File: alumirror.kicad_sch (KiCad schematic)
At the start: 36 parts, among them J1 USB_C_Receptacle_USB2.0_16P_2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, J2 USB_C_Receptacle_USB2.0_16P_2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, J3 USB_C_Receptacle_USB2.0_16P_2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, J4 USB_C_Receptacle_USB2.0_16P_2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, SW1 BOOT, U1 CH552T, U2 CH552T, U3 USBLC6-2P6, U4 USBLC6-2P6, U5 USBLC6-2P6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

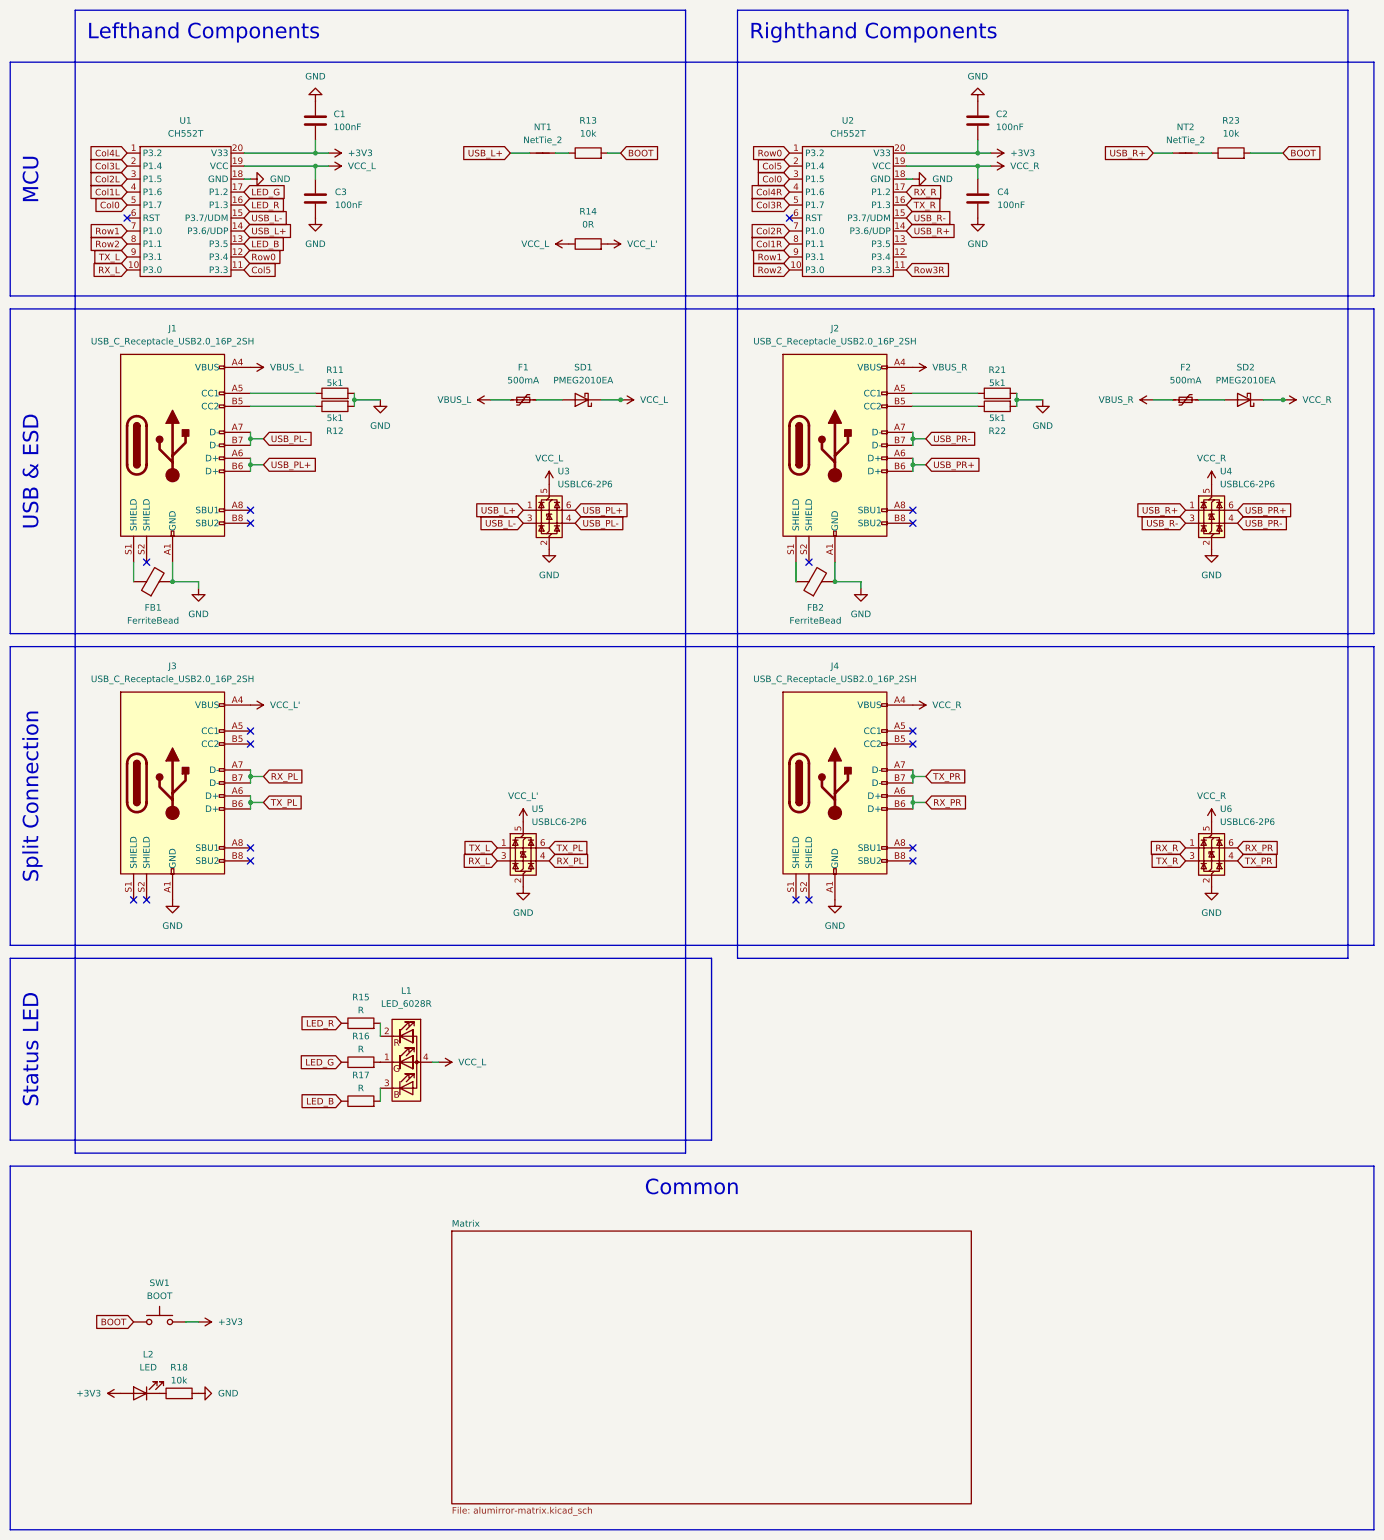
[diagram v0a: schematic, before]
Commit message: Rearrange components for better layout
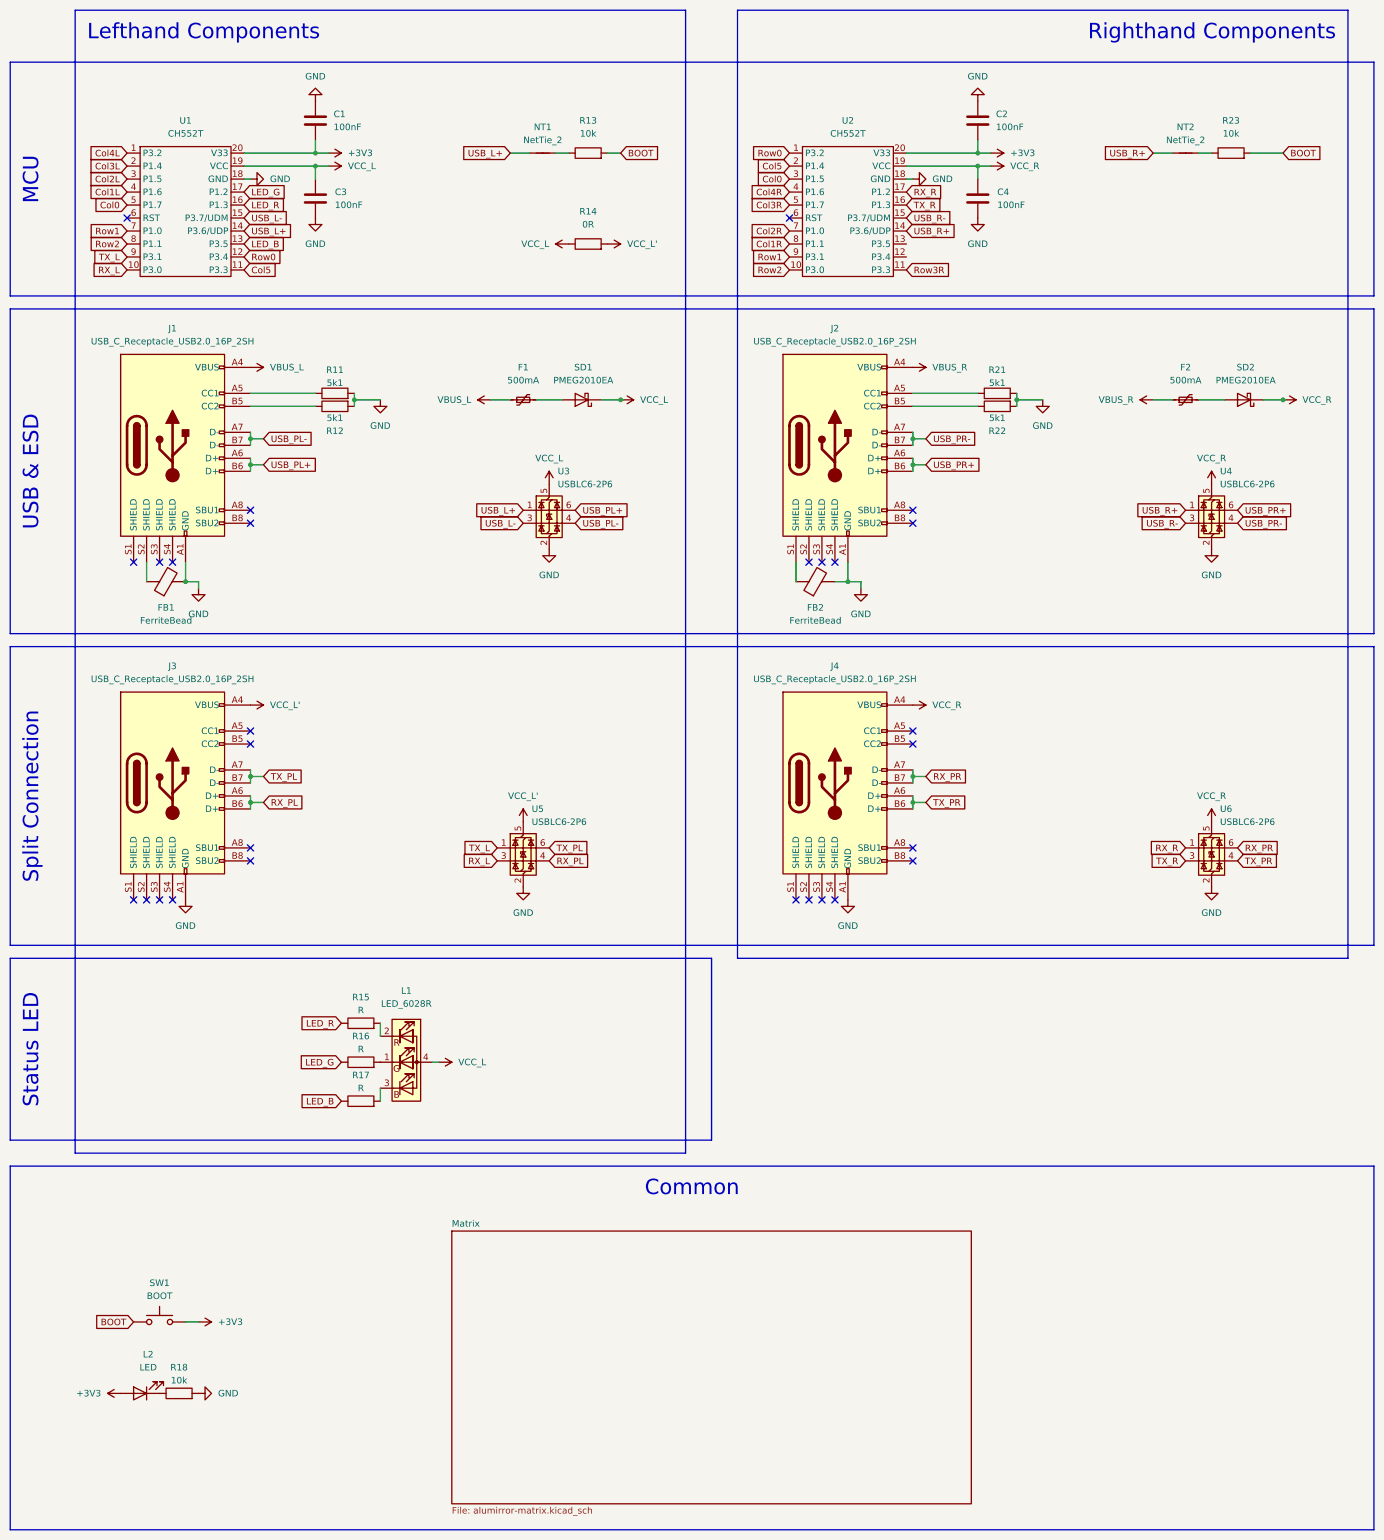
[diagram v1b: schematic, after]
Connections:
- net RX_PL: now also J3.A6 (D+), J3.B6 (D+); no longer J3.A7 (D-), J3.B7 (D-)
- net RX_PR: now also J4.A7 (D-), J4.B7 (D-); no longer J4.A6 (D+), J4.B6 (D+)
- net TX_PL: now also J3.A7 (D-), J3.B7 (D-); no longer J3.A6 (D+), J3.B6 (D+)
- net TX_PR: now also J4.A6 (D+), J4.B6 (D+); no longer J4.A7 (D-), J4.B7 (D-)
- net at FB1.1: now also J1.S2 (SHIELD); no longer J1.S1 (SHIELD)
- no-connect marks 20 -> 28
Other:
- moved on the sheet: FB1
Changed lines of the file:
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@@
 	)
 	(junction
-		(at 62.23 165.1)
+		(at 179.07 127)
 		(diameter 0)
 		(color 0 0 0 0)
 	)
 	(junction
-		(at 62.23 170.18)
+		(at 62.23 165.1)
 		(diameter 0)
 		(color 0 0 0 0)
 	)
 	(junction
-		(at 191.77 170.18)
+		(at 62.23 170.18)
 		(diameter 0)
 		(color 0 0 0 0)
 	)
 	(junction
-		(at 264.16 91.44)
+		(at 191.77 170.18)
 		(diameter 0)
 		(color 0 0 0 0)
 	)
 	(junction
-		(at 176.53 127)
+		(at 264.16 91.44)
 		(diameter 0)
 		(color 0 0 0 0)
@@
 	)
 	(junction
-		(at 46.99 127)
-		(diameter 0)
-		(color 0 0 0 0)
-	)
-	(junction
 		(at 134.62 91.44)
 		(diameter 0)
@@
 	)
 	(junction
+		(at 49.53 127)
+		(diameter 0)
+		(color 0 0 0 0)
+	)
+	(junction
 		(at 191.77 99.06)
 		(diameter 0)
@@
 	)
 	(no_connect
+		(at 173.99 189.23)
+	)
+	(no_connect
 		(at 168.91 189.23)
 	)
 	(no_connect
+		(at 44.45 123.19)
+	)
+	(no_connect
 		(at 62.23 156.21)
 	)
 	(no_connect
+		(at 176.53 123.19)
+	)
+	(no_connect
 		(at 171.45 189.23)
 	)
@@
 	)
 	(no_connect
+		(at 176.53 189.23)
+	)
+	(no_connect
 		(at 62.23 113.03)
 	)
@@
 	)
 	(no_connect
+		(at 46.99 123.19)
+	)
+	(no_connect
+		(at 44.45 189.23)
+	)
+	(no_connect
 		(at 191.77 156.21)
 	)
@@
 	)
 	(no_connect
-		(at 41.91 123.19)
-	)
-	(no_connect
 		(at 191.77 115.57)
 	)
@@
 	)
 	(no_connect
+		(at 39.37 123.19)
+	)
+	(no_connect
 		(at 191.77 113.03)
 	)
 	(no_connect
+		(at 173.99 123.19)
+	)
+	(no_connect
 		(at 62.23 179.07)
 	)
+	(no_connect
+		(at 46.99 189.23)
+	)
 	(wire
 		(pts
@@
 	(wire
 		(pts
-			(xy 176.53 123.19) (xy 176.53 127)
+			(xy 191.77 170.18) (xy 191.77 171.45)
 		)
 		(stroke
@@
 	(wire
 		(pts
-			(xy 191.77 170.18) (xy 191.77 171.45)
+			(xy 64.77 99.06) (xy 62.23 99.06)
 		)
 		(stroke
@@
 	(wire
 		(pts
-			(xy 64.77 99.06) (xy 62.23 99.06)
+			(xy 62.23 97.79) (xy 62.23 99.06)
 		)
 		(stroke
@@
 	(wire
 		(pts
-			(xy 62.23 97.79) (xy 62.23 99.06)
+			(xy 191.77 163.83) (xy 191.77 165.1)
 		)
 		(stroke
@@
 	(wire
 		(pts
-			(xy 191.77 163.83) (xy 191.77 165.1)
+			(xy 62.23 99.06) (xy 62.23 100.33)
 		)
 		(stroke
@@
 	(wire
 		(pts
-			(xy 62.23 99.06) (xy 62.23 100.33)
+			(xy 194.31 170.18) (xy 191.77 170.18)
 		)
 		(stroke
@@
 	(wire
 		(pts
-			(xy 194.31 170.18) (xy 191.77 170.18)
+			(xy 217.17 91.44) (xy 212.09 91.44)
 		)
 		(stroke
@@
 	(wire
 		(pts
-			(xy 217.17 91.44) (xy 212.09 91.44)
+			(xy 41.91 123.19) (xy 41.91 127)
 		)
 		(stroke
@@
 	(wire
 		(pts
-			(xy 181.61 127) (xy 176.53 127)
+			(xy 181.61 127) (xy 179.07 127)
 		)
 		(stroke
@@
 	(wire
 		(pts
-			(xy 46.99 123.19) (xy 46.99 127)
+			(xy 204.47 43.18) (xy 207.01 43.18)
 		)
 		(stroke
@@
 	(wire
 		(pts
-			(xy 204.47 43.18) (xy 207.01 43.18)
+			(xy 194.31 99.06) (xy 191.77 99.06)
 		)
 		(stroke
@@
 	(wire
 		(pts
-			(xy 194.31 99.06) (xy 191.77 99.06)
+			(xy 179.07 127) (xy 176.53 127)
 		)
 		(stroke
@@
 	(wire
 		(pts
-			(xy 52.07 127) (xy 46.99 127)
+			(xy 52.07 127) (xy 49.53 127)
 		)
 		(stroke
@@
 	(wire
 		(pts
-			(xy 39.37 127) (xy 39.37 123.19)
-		)
-		(stroke
-			(width 0)
-			(type default)
-		)
-	)
-	(wire
-		(pts
 			(xy 64.77 165.1) (xy 62.23 165.1)
 		)
@@
 	(wire
 		(pts
+			(xy 49.53 123.19) (xy 49.53 127)
+		)
+		(stroke
+			(width 0)
+			(type default)
+		)
+	)
+	(wire
+		(pts
 			(xy 74.93 43.18) (xy 77.47 43.18)
 		)
@@
 	(wire
 		(pts
+			(xy 179.07 123.19) (xy 179.07 127)
+		)
+		(stroke
+			(width 0)
+			(type default)
+		)
+	)
+	(wire
+		(pts
 			(xy 74.93 40.64) (xy 74.93 43.18)
 		)
@@
 				(size 3 3)
 			)
-			(justify left top)
+			(justify right top)
 		)
 	)
@@
 	(global_label "RX_PL"
 		(shape input)
-		(at 64.77 165.1 0)
+		(at 64.77 170.18 0)
 		(fields_autoplaced yes)
 		(effects
@@
 		)
 		(property "Intersheetrefs" "${INTERSHEET_REFS}"
-			(at 73.5004 165.1 0)
+			(at 73.5004 170.18 0)
 			(effects
 				(font
@@
 	(global_label "TX_PL"
 		(shape input)
-		(at 64.77 170.18 0)
+		(at 64.77 165.1 0)
 		(fields_autoplaced yes)
 		(effects
@@
 		)
 		(property "Intersheetrefs" "${INTERSHEET_REFS}"
-			(at 73.198 170.18 0)
+			(at 73.198 165.1 0)
 			(effects
 				(font
@@
 	(global_label "RX_PR"
 		(shape input)
-		(at 194.31 170.18 0)
+		(at 194.31 165.1 0)
 		(fields_autoplaced yes)
 		(effects
@@
 		)
 		(property "Intersheetrefs" "${INTERSHEET_REFS}"
-			(at 203.2823 170.18 0)
+			(at 203.2823 165.1 0)
 			(effects
 				(font
@@
 	(global_label "TX_PR"
 		(shape input)
-		(at 194.31 165.1 0)
+		(at 194.31 170.18 0)
 		(fields_autoplaced yes)
 		(effects
@@
 		)
 		(property "Intersheetrefs" "${INTERSHEET_REFS}"
-			(at 202.9799 165.1 0)
+			(at 202.9799 170.18 0)
 			(effects
 				(font
@@
 		(pin "B7"
 		)
+		(pin "S3"
+		)
+		(pin "S4"
+		)
 		(instances
 			(project "alumirror"
@@
 		(pin "B7"
 		)
+		(pin "S3"
+		)
+		(pin "S4"
+		)
 		(instances
 			(project "alumirror"
@@
 	(symbol
 		(lib_id "Device:FerriteBead")
-		(at 43.18 127 90)
+		(at 45.72 127 90)
 		(unit 1)
 		(exclude_from_sim no)
@@
 		(dnp no)
 		(property "Reference" "FB1"
-			(at 43.18 132.08 90)
+			(at 45.72 132.08 90)
 			(effects
 				(font
@@
 		)
 		(property "Value" "FerriteBead"
-			(at 43.18 134.62 90)
+			(at 45.72 134.62 90)
 			(effects
 				(font
@@
 		)
 		(property "Footprint" "Inductor_SMD:L_0805_2012Metric"
-			(at 43.18 128.778 90)
+			(at 45.72 128.778 90)
 			(effects
 				(font
@@
 		)
 		(property "Datasheet" "~"
-			(at 43.18 127 0)
+			(at 45.72 127 0)
 			(effects
 				(font
@@
 		)
 		(property "Description" "Ferrite bead"
-			(at 43.18 127 0)
+			(at 45.72 127 0)
 			(effects
 				(font
@@
 	(symbol
 		(lib_id "power:GND")
-		(at 176.53 189.23 0)
+		(at 179.07 189.23 0)
 		(unit 1)
 		(exclude_from_sim no)
@@
 		(fields_autoplaced yes)
 		(property "Reference" "#PWR033"
-			(at 176.53 195.58 0)
+			(at 179.07 195.58 0)
 			(effects
 				(font
@@
 		)
 		(property "Value" "GND"
-			(at 176.53 194.31 0)
+			(at 179.07 194.31 0)
 			(effects
 				(font
@@
 		)
 		(property "Footprint" ""
-			(at 176.53 189.23 0)
+			(at 179.07 189.23 0)
 			(effects
 				(font
@@
 		)
 		(property "Datasheet" ""
-			(at 176.53 189.23 0)
+			(at 179.07 189.23 0)
 			(effects
 				(font
@@
 		)
 		(property "Description" "Power symbol creates a global label with name \"GND\" , ground"
-			(at 176.53 189.23 0)
+			(at 179.07 189.23 0)
 			(effects
 				(font
@@
 		(pin "B7"
 		)
+		(pin "S3"
+		)
+		(pin "S4"
+		)
 		(instances
 			(project ""
@@
 	(symbol
 		(lib_id "power:GND")
-		(at 46.99 189.23 0)
+		(at 49.53 189.23 0)
 		(unit 1)
 		(exclude_from_sim no)
@@
 		(fields_autoplaced yes)
 		(property "Reference" "#PWR015"
-			(at 46.99 195.58 0)
+			(at 49.53 195.58 0)
 			(effects
 				(font
@@
 		)
 		(property "Value" "GND"
-			(at 46.99 194.31 0)
+			(at 49.53 194.31 0)
 			(effects
 				(font
@@
 		)
 		(property "Footprint" ""
-			(at 46.99 189.23 0)
+			(at 49.53 189.23 0)
 			(effects
 				(font
@@
 		)
 		(property "Datasheet" ""
-			(at 46.99 189.23 0)
+			(at 49.53 189.23 0)
 			(effects
 				(font
@@
 		)
 		(property "Description" "Power symbol creates a global label with name \"GND\" , ground"
-			(at 46.99 189.23 0)
+			(at 49.53 189.23 0)
 			(effects
 				(font
@@
 		(pin "B7"
 		)
+		(pin "S3"
+		)
+		(pin "S4"
+		)
 		(instances

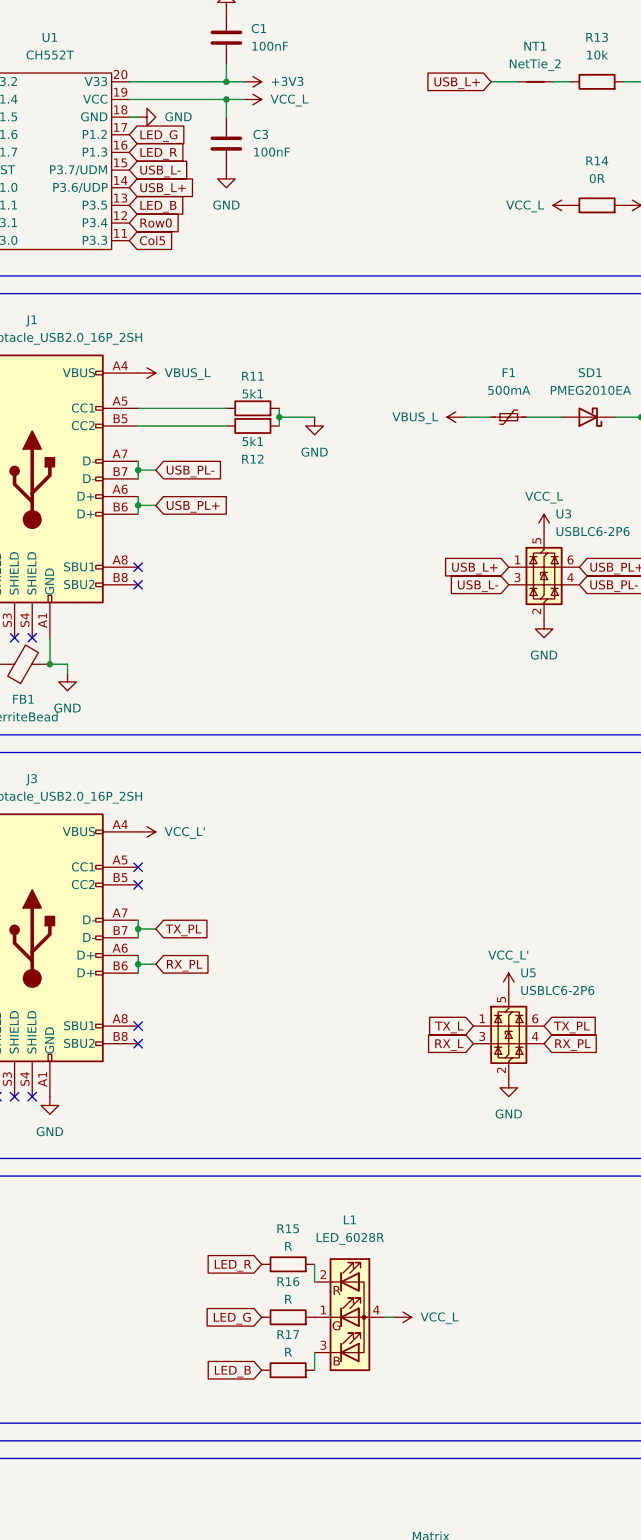
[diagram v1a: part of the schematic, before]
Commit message: Replace three-colour RGB LED with SK6812MINI-E
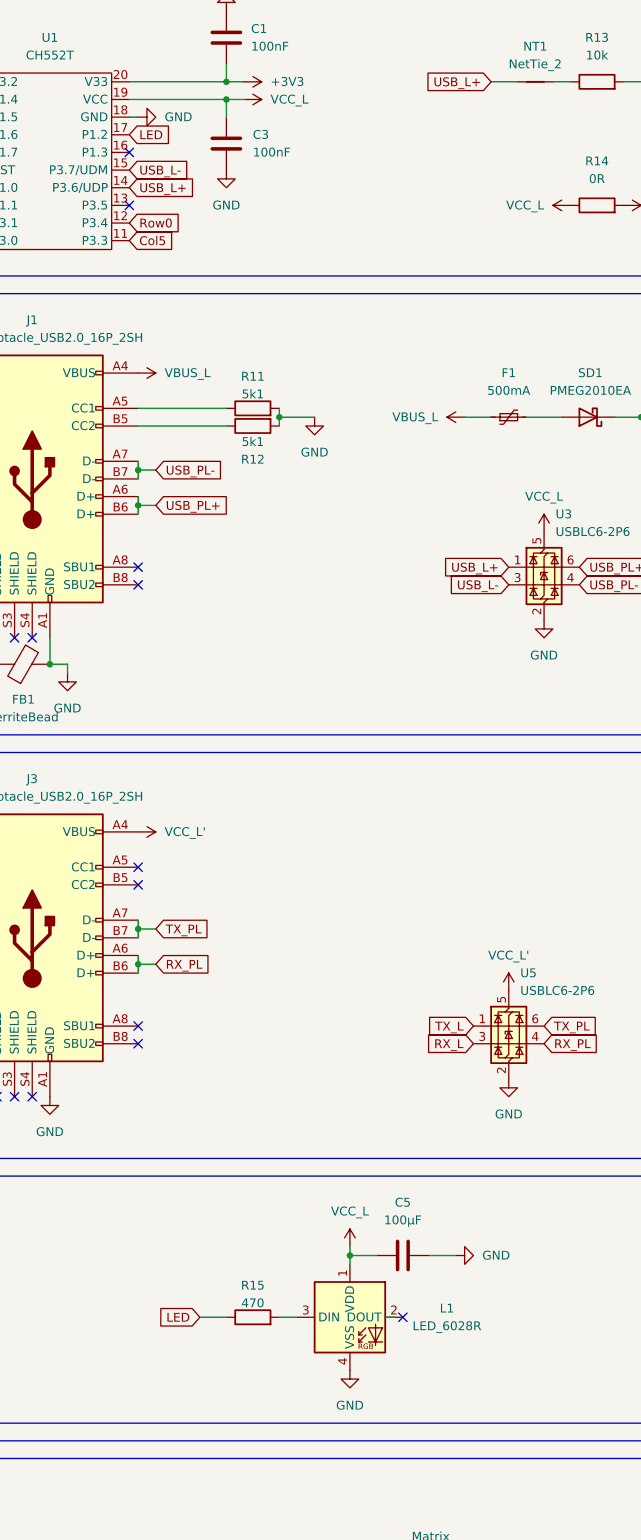
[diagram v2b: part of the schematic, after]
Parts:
- removed R16, R17: R, Project Library:R_0603_1608Metric_Mod, symbol Device:R
- added C5: 100µF, Capacitor_SMD:C_0603_1608Metric, symbol Device:C
- L1: symbol PCM_marbastlib-various:LED_6028R -> PCM_marbastlib-various:SK6812MINI-E
- R15: value R -> 470; DigiKey (none) -> 311-5.10KHR; LCSC (none) -> C23186
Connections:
- net GND: now also L1.4 (VSS), C5.2
- net VCC_L: now also L1.1 (VDD), C5.1; no longer L1.4 (A)
- net at L1.3 (DIN): now also R15.2
- net at L1.2 (DOUT): no longer R15.2
- net LED_B: no longer names the net of U1.13 (P3.5)
- net LED_G renamed LED
- net LED: now also R15.1
- net LED_R: no longer names the net of U1.16 (P1.3)
- net LED_R: no longer R15.1
- no-connect marks 28 -> 31

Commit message: Add custom SOT-666 footprint
Footprint has ground routing and 3D cutout
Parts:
- U3, U4, U5, U6: footprint Package_TO_SOT_SMD:SOT-666 -> Project Library:SOT-666_Mod
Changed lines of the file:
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@@
 			)
 		)
-		(property "Footprint" "Package_TO_SOT_SMD:SOT-666"
+		(property "Footprint" "Project Library:SOT-666_Mod"
 			(at 251.206 185.801 0)
 			(effects
@@
 			)
 		)
-		(property "Footprint" "Package_TO_SOT_SMD:SOT-666"
+		(property "Footprint" "Project Library:SOT-666_Mod"
 			(at 116.586 185.801 0)
 			(effects
@@
 			)
 		)
-		(property "Footprint" "Package_TO_SOT_SMD:SOT-666"
+		(property "Footprint" "Project Library:SOT-666_Mod"
 			(at 251.206 119.761 0)
 			(effects
@@
 			)
 		)
-		(property "Footprint" "Package_TO_SOT_SMD:SOT-666"
+		(property "Footprint" "Project Library:SOT-666_Mod"
 			(at 121.666 119.761 0)
 			(effects
